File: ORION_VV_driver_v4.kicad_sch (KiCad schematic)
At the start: 154 parts, among them J1 Conn_01x01, J10 Conn_01x01, J11 Conn_01x02, J12 Conn_01x05, J13 Conn_01x05, J14 Conn_01x01, J15 Conn_01x02, J16 Conn_01x01, J17 Conn_01x01, J18 Conn_01x01, J19 Conn_01x01, J2 Conn_01x04, J3 Conn_01x04, J4 Conn_01x06, J5 Conn_01x07, J6 Conn_01x07, J7 Conn_01x01, J8 Conn_01x01, J9 Conn_01x01, Q1 IRF8721PBF-1, Q10 IRF8721PBF-1, Q11 IRF8721PBF-1, Q12 IRF8721PBF-1, Q2 IRF8721PBF-1, Q3 IRF8721PBF-1, Q4 IRF8721PBF-1, Q5 IRF8721PBF-1, Q6 IRF8721PBF-1, Q7 IRF8721PBF-1, Q8 IRF8721PBF-1, Q9 IRF8721PBF-1, SW1 SW_Push, SW2 SW_Push, SW3 SW_Push, SW4 SW_Push, SW5 SW_Push, U1 BD9G101G, U2 L78L33_SOT89, U3 MAX3051, U5 ZXCT108x, U6 ZXCT108x, Y1 Resonator

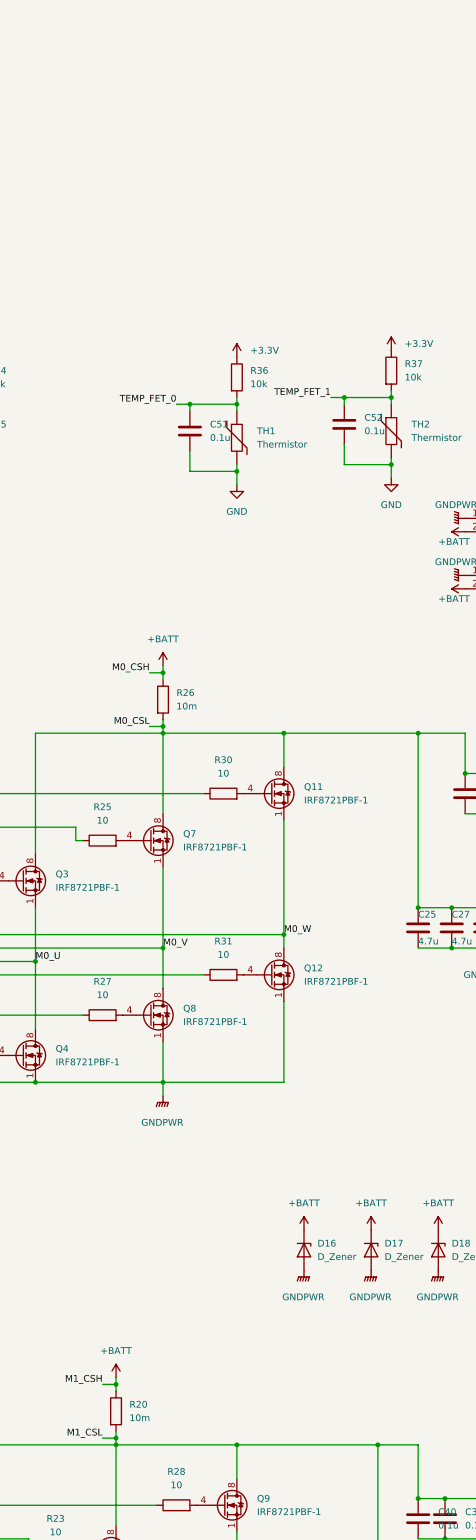
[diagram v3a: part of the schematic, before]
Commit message: パワー系チェック用のテストパッド追加
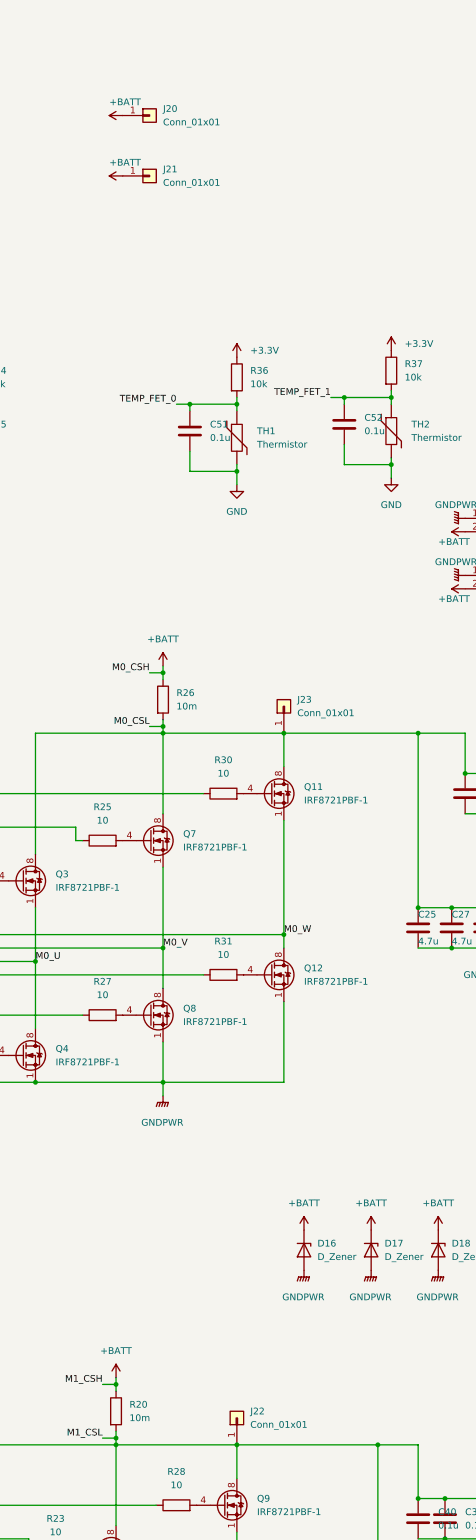
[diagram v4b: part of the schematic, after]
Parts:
- added J20, J21, J22, J23: Conn_01x01, TestPoint:TestPoint_Loop_D2.60mm_Drill0.9mm_Beaded, symbol Connector_Generic:Conn_01x01
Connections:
- net +BATT: now also J20.1 (Pin_1), J21.1 (Pin_1)
- net M0_CSL: now also J23.1 (Pin_1)
- net M1_CSL: now also J22.1 (Pin_1)
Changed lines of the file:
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@@
     (pin "9")
   )
+  (symbol (lib_id "Connector_Generic:Conn_01x01") (at 492.76 149.86 90) (unit 1)
+    (in_bom yes) (on_board yes) (fields_autoplaced)
+    (property "Reference" "J23" (id 0) (at 495.3 148.5899 90)
+      (effects (font (size 1.27 1.27)) (justify right))
+    )
+    (property "Value" "Conn_01x01" (id 1) (at 495.3 151.1299 90)
+      (effects (font (size 1.27 1.27)) (justify right))
+    )
+    (property "Footprint" "TestPoint:TestPoint_Loop_D2.60mm_Drill0.9mm_Beaded" (id 2) (at 492.76 149.86 0)
+      (effects (font (size 1.27 1.27)) hide)
+    )
+    (property "Datasheet" "~" (id 3) (at 492.76 149.86 0)
+      (effects (font (size 1.27 1.27)) hide)
+    )
+    (pin "1")
+  )
   (symbol (lib_id "power:GND") (at 434.34 105.41 0) (unit 1)
     (in_bom yes) (on_board yes) (fields_autoplaced)
@@
     (pin "1")
   )
+  (symbol (lib_id "Connector_Generic:Conn_01x01") (at 467.36 49.53 0) (unit 1)
+    (in_bom yes) (on_board yes) (fields_autoplaced)
+    (property "Reference" "J21" (id 0) (at 469.9 48.2599 0)
+      (effects (font (size 1.27 1.27)) (justify left))
+    )
+    (property "Value" "Conn_01x01" (id 1) (at 469.9 50.7999 0)
+      (effects (font (size 1.27 1.27)) (justify left))
+    )
+    (property "Footprint" "TestPoint:TestPoint_Loop_D2.60mm_Drill0.9mm_Beaded" (id 2) (at 467.36 49.53 0)
+      (effects (font (size 1.27 1.27)) hide)
+    )
+    (property "Datasheet" "~" (id 3) (at 467.36 49.53 0)
+      (effects (font (size 1.27 1.27)) hide)
+    )
+    (pin "1")
+  )
   (symbol (lib_id "Device:R") (at 119.38 105.41 180) (unit 1)
     (in_bom yes) (on_board yes) (fields_autoplaced)
@@
     (pin "2")
   )
+  (symbol (lib_id "power:+BATT") (at 462.28 49.53 90) (unit 1)
+    (in_bom yes) (on_board yes)
+    (property "Reference" "#PWR065" (id 0) (at 466.09 49.53 0)
+      (effects (font (size 1.27 1.27)) hide)
+    )
+    (property "Value" "+BATT" (id 1) (at 459.74 46.99 90)
+      (effects (font (size 1.27 1.27)) (justify right))
+    )
+    (property "Footprint" "" (id 2) (at 462.28 49.53 0)
+      (effects (font (size 1.27 1.27)) hide)
+    )
+    (property "Datasheet" "" (id 3) (at 462.28 49.53 0)
+      (effects (font (size 1.27 1.27)) hide)
+    )
+    (pin "1")
+  )
   (symbol (lib_id "power:+BATT") (at 527.05 127.635 90) (unit 1)
     (in_bom yes) (on_board yes)
@@
     (pin "2")
   )
+  (symbol (lib_id "Connector_Generic:Conn_01x01") (at 483.87 284.48 90) (unit 1)
+    (in_bom yes) (on_board yes) (fields_autoplaced)
+    (property "Reference" "J22" (id 0) (at 486.41 283.2099 90)
+      (effects (font (size 1.27 1.27)) (justify right))
+    )
+    (property "Value" "Conn_01x01" (id 1) (at 486.41 285.7499 90)
+      (effects (font (size 1.27 1.27)) (justify right))
+    )
+    (property "Footprint" "TestPoint:TestPoint_Loop_D2.60mm_Drill0.9mm_Beaded" (id 2) (at 483.87 284.48 0)
+      (effects (font (size 1.27 1.27)) hide)
+    )
+    (property "Datasheet" "~" (id 3) (at 483.87 284.48 0)
+      (effects (font (size 1.27 1.27)) hide)
+    )
+    (pin "1")
+  )
   (symbol (lib_id "power:+3.3V") (at 151.13 334.01 0) (unit 1)
     (in_bom yes) (on_board yes) (fields_autoplaced)
@@
     (pin "8")
   )
+  (symbol (lib_id "Connector_Generic:Conn_01x01") (at 467.36 38.1 0) (unit 1)
+    (in_bom yes) (on_board yes) (fields_autoplaced)
+    (property "Reference" "J20" (id 0) (at 469.9 36.8299 0)
+      (effects (font (size 1.27 1.27)) (justify left))
+    )
+    (property "Value" "Conn_01x01" (id 1) (at 469.9 39.3699 0)
+      (effects (font (size 1.27 1.27)) (justify left))
+    )
+    (property "Footprint" "TestPoint:TestPoint_Loop_D2.60mm_Drill0.9mm_Beaded" (id 2) (at 467.36 38.1 0)
+      (effects (font (size 1.27 1.27)) hide)
+    )
+    (property "Datasheet" "~" (id 3) (at 467.36 38.1 0)
+      (effects (font (size 1.27 1.27)) hide)
+    )
+    (pin "1")
+  )
   (symbol (lib_id "power:+BATT") (at 387.35 83.82 0) (unit 1)
     (in_bom yes) (on_board yes) (fields_autoplaced)
@@
     (pin "2")
   )
+  (symbol (lib_id "power:+BATT") (at 462.28 38.1 90) (unit 1)
+    (in_bom yes) (on_board yes)
+    (property "Reference" "#PWR064" (id 0) (at 466.09 38.1 0)
+      (effects (font (size 1.27 1.27)) hide)
+    )
+    (property "Value" "+BATT" (id 1) (at 459.74 35.56 90)
+      (effects (font (size 1.27 1.27)) (justify right))
+    )
+    (property "Footprint" "" (id 2) (at 462.28 38.1 0)
+      (effects (font (size 1.27 1.27)) hide)
+    )
+    (property "Datasheet" "" (id 3) (at 462.28 38.1 0)
+      (effects (font (size 1.27 1.27)) hide)
+    )
+    (pin "1")
+  )
   (symbol (lib_id "power:GNDPWR") (at 563.88 168.91 270) (unit 1)
     (in_bom yes) (on_board yes) (fields_autoplaced)
@@
       (reference "#PWR063") (unit 1) (value "GNDPWR") (footprint "")
     )
+    (path "/c9240a0d-41cb-42e8-896a-38e65d5324d9"
+      (reference "#PWR064") (unit 1) (value "+BATT") (footprint "")
+    )
+    (path "/2f6c3325-3a12-4f6d-b093-fea5de80154c"
+      (reference "#PWR065") (unit 1) (value "+BATT") (footprint "")
+    )
     (path "/3e85acbf-2797-4de8-aa88-8f714b41f622"
       (reference "#PWR066") (unit 1) (value "GNDPWR") (footprint "")
@@
       (reference "J19") (unit 1) (value "Conn_01x01") (footprint "TestPoint:TestPoint_Loop_D2.60mm_Drill0.9mm_Beaded")
     )
+    (path "/c3424e1f-6b87-4540-afd4-d575db79cb3e"
+      (reference "J20") (unit 1) (value "Conn_01x01") (footprint "TestPoint:TestPoint_Loop_D2.60mm_Drill0.9mm_Beaded")
+    )
+    (path "/1faee419-d66b-4115-85d6-2e574c968b99"
+      (reference "J21") (unit 1) (value "Conn_01x01") (footprint "TestPoint:TestPoint_Loop_D2.60mm_Drill0.9mm_Beaded")
+    )
+    (path "/4d979704-3e9d-41a8-a1f8-b02103d32b4e"
+      (reference "J22") (unit 1) (value "Conn_01x01") (footprint "TestPoint:TestPoint_Loop_D2.60mm_Drill0.9mm_Beaded")
+    )
+    (path "/1e76d7cf-34a0-4e1e-9005-e997a512ecd1"
+      (reference "J23") (unit 1) (value "Conn_01x01") (footprint "TestPoint:TestPoint_Loop_D2.60mm_Drill0.9mm_Beaded")
+    )
     (path "/ed816bbd-1d2b-4396-aa8f-2fdb60409bd0"

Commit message: 盆栽
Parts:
- SW1, SW2, SW3, SW4, SW5: footprint Button_Switch_SMD:SW_Push_1P1T_NO_CK_KMR2 -> Button_Switch_SMD:SW_Push_SPST_NO_Alps_SKRK
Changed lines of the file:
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@@
       (effects (font (size 1.27 1.27)) (justify right))
     )
-    (property "Footprint" "Button_Switch_SMD:SW_Push_1P1T_NO_CK_KMR2" (id 2) (at 149.86 175.26 0)
+    (property "Footprint" "Button_Switch_SMD:SW_Push_SPST_NO_Alps_SKRK" (id 2) (at 149.86 175.26 0)
       (effects (font (size 1.27 1.27)) hide)
     )
@@
       (effects (font (size 1.27 1.27)) (justify right))
     )
-    (property "Footprint" "Button_Switch_SMD:SW_Push_1P1T_NO_CK_KMR2" (id 2) (at 124.46 175.26 0)
+    (property "Footprint" "Button_Switch_SMD:SW_Push_SPST_NO_Alps_SKRK" (id 2) (at 124.46 175.26 0)
       (effects (font (size 1.27 1.27)) hide)
     )
@@
       (effects (font (size 1.27 1.27)) (justify right))
     )
-    (property "Footprint" "Button_Switch_SMD:SW_Push_1P1T_NO_CK_KMR2" (id 2) (at 162.56 175.26 0)
+    (property "Footprint" "Button_Switch_SMD:SW_Push_SPST_NO_Alps_SKRK" (id 2) (at 162.56 175.26 0)
       (effects (font (size 1.27 1.27)) hide)
     )
@@
       (effects (font (size 1.27 1.27)) (justify right))
     )
-    (property "Footprint" "Button_Switch_SMD:SW_Push_1P1T_NO_CK_KMR2" (id 2) (at 137.16 175.26 0)
+    (property "Footprint" "Button_Switch_SMD:SW_Push_SPST_NO_Alps_SKRK" (id 2) (at 137.16 175.26 0)
       (effects (font (size 1.27 1.27)) hide)
     )
@@
       (effects (font (size 1.27 1.27)) (justify right))
     )
-    (property "Footprint" "Button_Switch_SMD:SW_Push_1P1T_NO_CK_KMR2" (id 2) (at 139.7 152.4 0)
+    (property "Footprint" "Button_Switch_SMD:SW_Push_SPST_NO_Alps_SKRK" (id 2) (at 139.7 152.4 0)
       (effects (font (size 1.27 1.27)) hide)
     )
@@
     )
     (path "/f04c5629-5bf3-44eb-a56f-798942d2dd39"
-      (reference "SW1") (unit 1) (value "SW_Push") (footprint "Button_Switch_SMD:SW_Push_1P1T_NO_CK_KMR2")
+      (reference "SW1") (unit 1) (value "SW_Push") (footprint "Button_Switch_SMD:SW_Push_SPST_NO_Alps_SKRK")
     )
     (path "/594944ba-bd9b-4b6d-9e71-4ac446b68377"
-      (reference "SW2") (unit 1) (value "SW_Push") (footprint "Button_Switch_SMD:SW_Push_1P1T_NO_CK_KMR2")
+      (reference "SW2") (unit 1) (value "SW_Push") (footprint "Button_Switch_SMD:SW_Push_SPST_NO_Alps_SKRK")
     )
     (path "/ad3fd8cb-0d5a-405b-84ad-3acc644abc95"
-      (reference "SW3") (unit 1) (value "SW_Push") (footprint "Button_Switch_SMD:SW_Push_1P1T_NO_CK_KMR2")
+      (reference "SW3") (unit 1) (value "SW_Push") (footprint "Button_Switch_SMD:SW_Push_SPST_NO_Alps_SKRK")
     )
     (path "/58b172b7-39b5-4f8f-8535-fa70dec0551b"
-      (reference "SW4") (unit 1) (value "SW_Push") (footprint "Button_Switch_SMD:SW_Push_1P1T_NO_CK_KMR2")
+      (reference "SW4") (unit 1) (value "SW_Push") (footprint "Button_Switch_SMD:SW_Push_SPST_NO_Alps_SKRK")
     )
     (path "/69f873b8-f467-4de4-a60f-a6a76fbbec87"
-      (reference "SW5") (unit 1) (value "SW_Push") (footprint "Button_Switch_SMD:SW_Push_1P1T_NO_CK_KMR2")
+      (reference "SW5") (unit 1) (value "SW_Push") (footprint "Button_Switch_SMD:SW_Push_SPST_NO_Alps_SKRK")
     )
     (path "/d477e77e-c35c-4390-a96e-4bbfc643dd97"

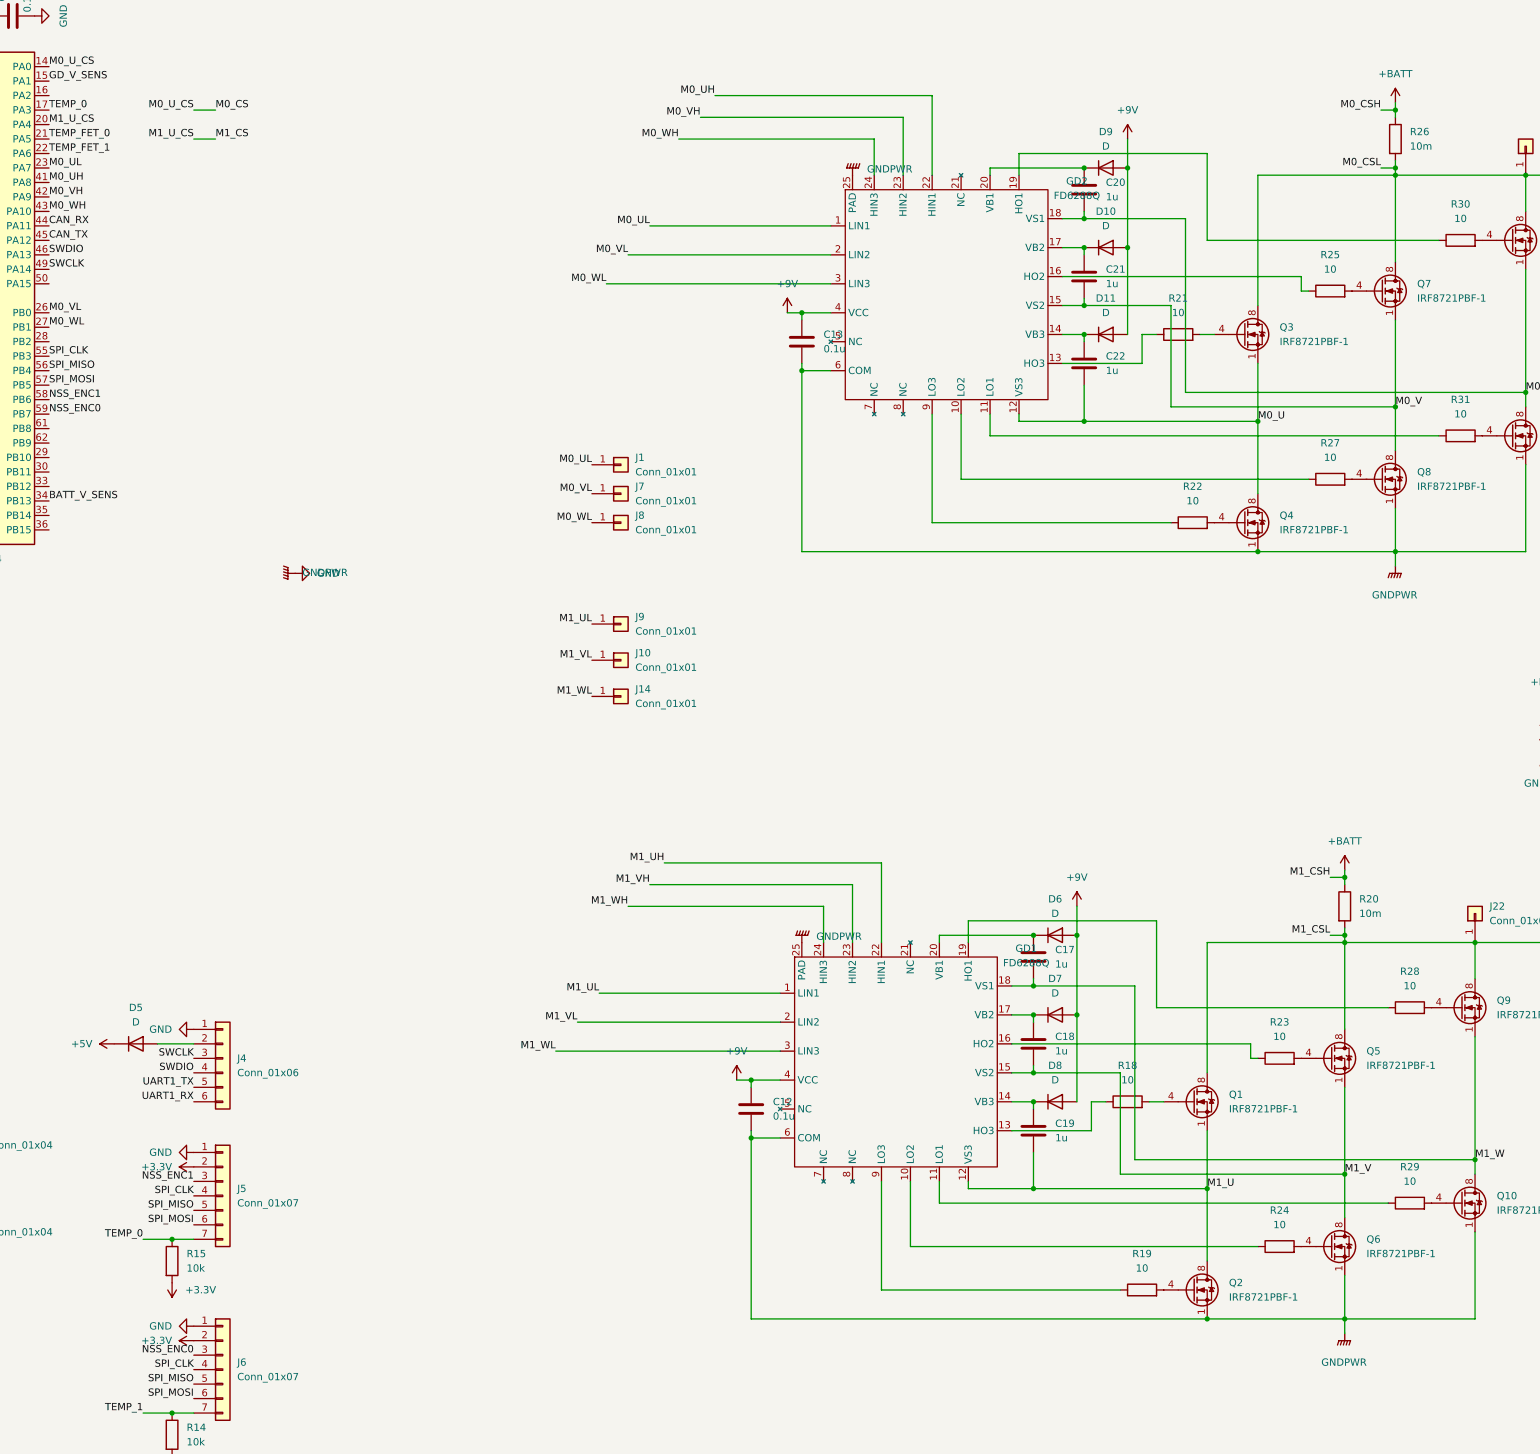
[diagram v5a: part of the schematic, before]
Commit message: エンコーダ電源にFB追加、GD電源に0Ω抵抗追加
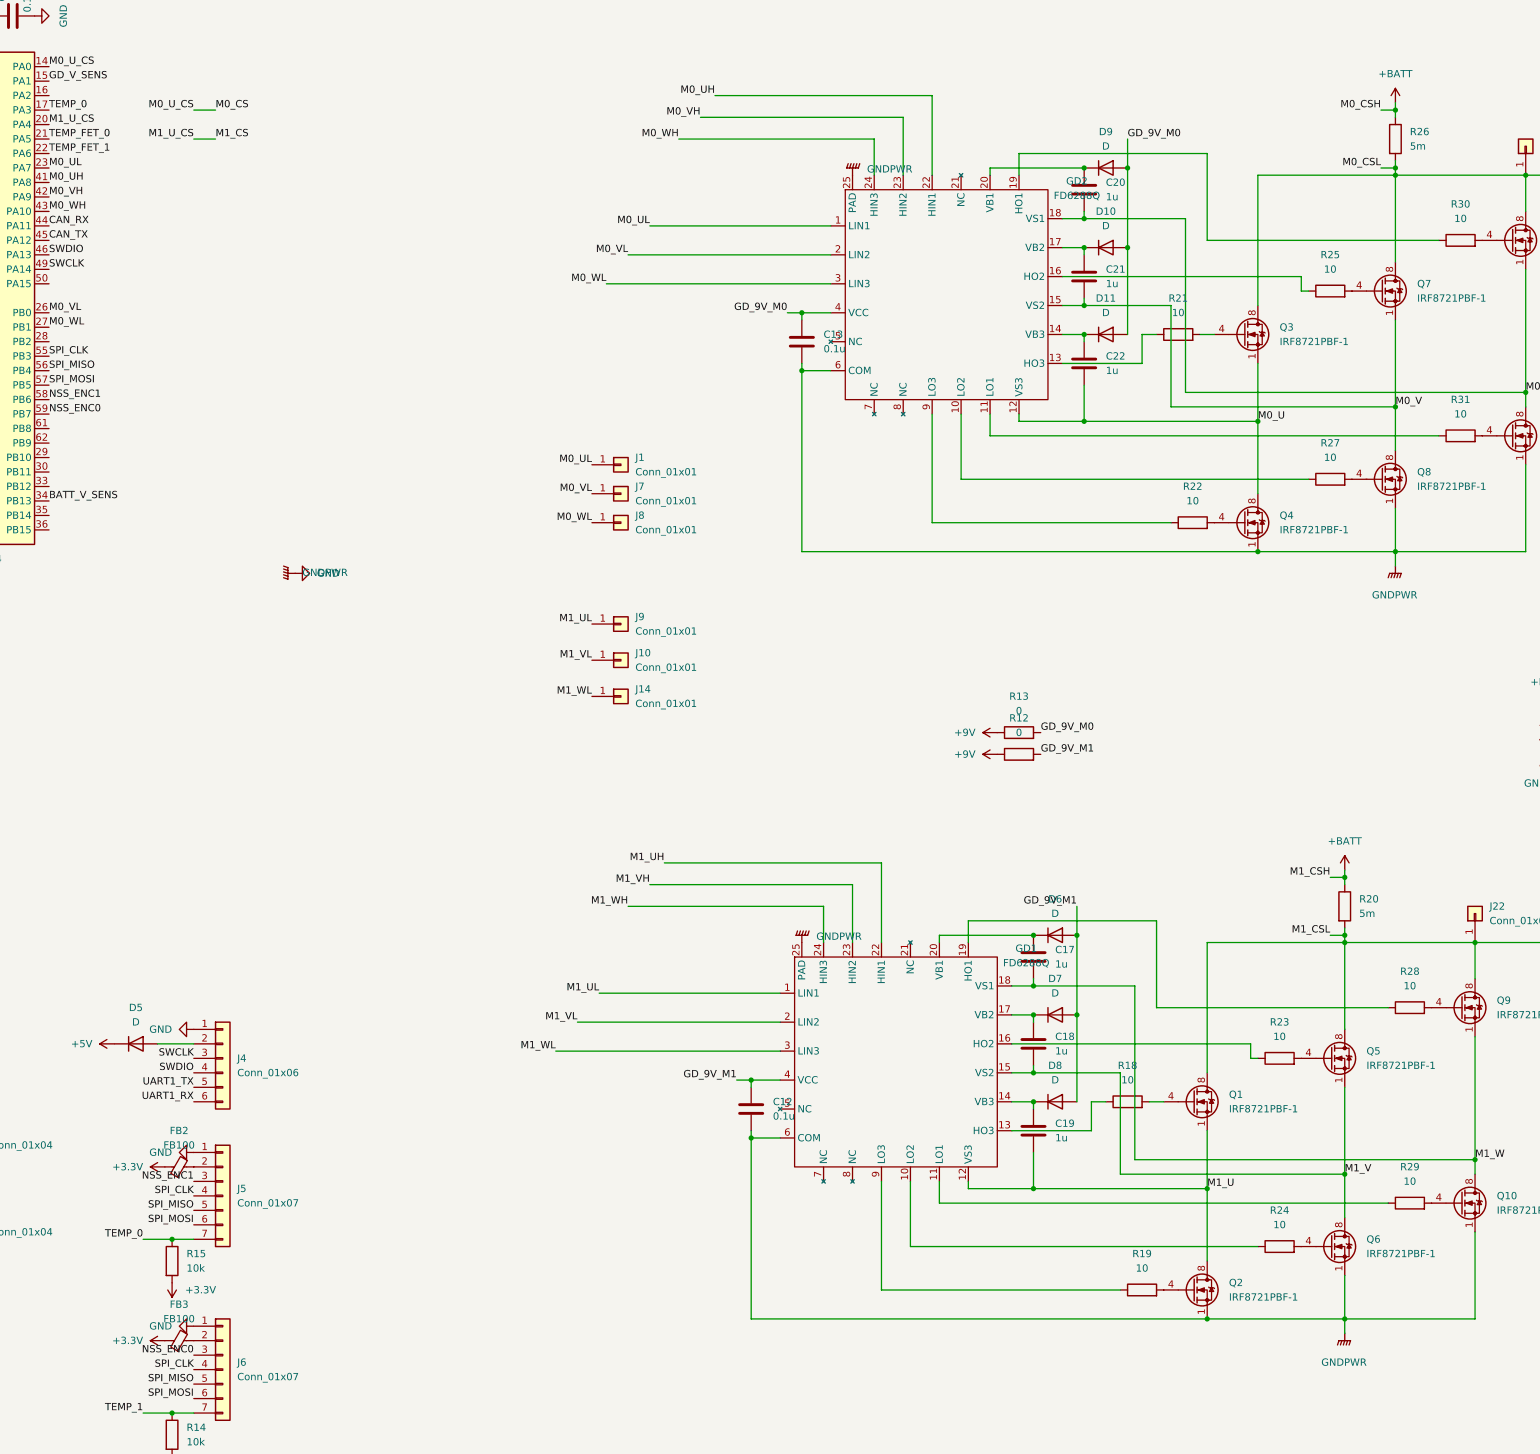
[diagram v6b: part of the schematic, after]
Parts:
- added FB2, FB3: FB100, Resistor_SMD:R_0603_1608Metric, symbol Device:FerriteBead_Small
- added R12, R13: 0, Resistor_SMD:R_0603_1608Metric, symbol Device:R
- R20, R26: value 10m -> 5m
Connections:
- net +3V3: now also FB2.1, FB3.1; no longer J5.2 (Pin_2), J6.2 (Pin_2)
- net +9V: now also R12.1, R13.1; no longer C12.2, C13.2, D10.2 (A), D11.2 (A), D6.2 (A), D7.2 (A), D8.2 (A), D9.2 (A), GD1.4 (VCC), GD2.4 (VCC)
- new net: FB3.2, J6.2 (Pin_2)
- new net: FB2.2, J5.2 (Pin_2)
- new net GD_9V_M0: C13.2, D10.2 (A), D11.2 (A), D9.2 (A), GD2.4 (VCC), R13.2
- new net GD_9V_M1: C12.2, D6.2 (A), D7.2 (A), D8.2 (A), GD1.4 (VCC), R12.2
